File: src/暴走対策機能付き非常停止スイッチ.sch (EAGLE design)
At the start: 13 parts, among them T2 一般的なトランジスタ

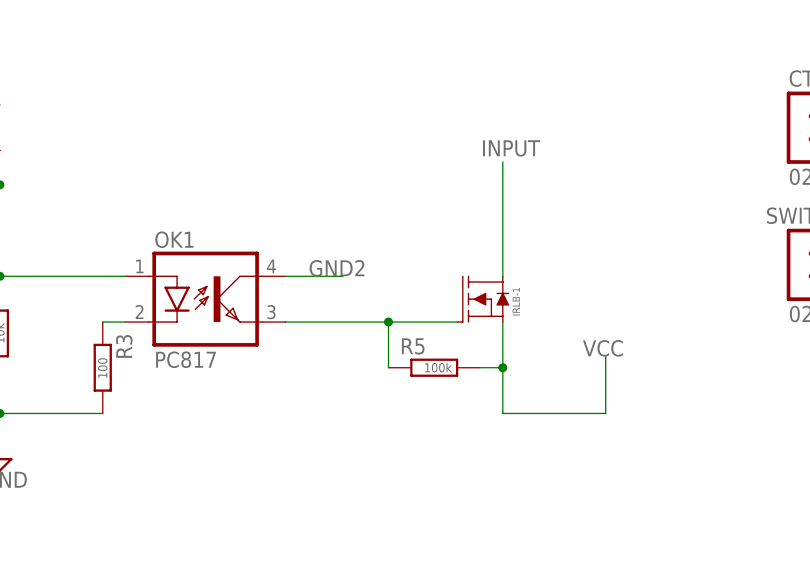
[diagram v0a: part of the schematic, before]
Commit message: 暴走対策機能付き非常停止スイッチの回路のガバを修復
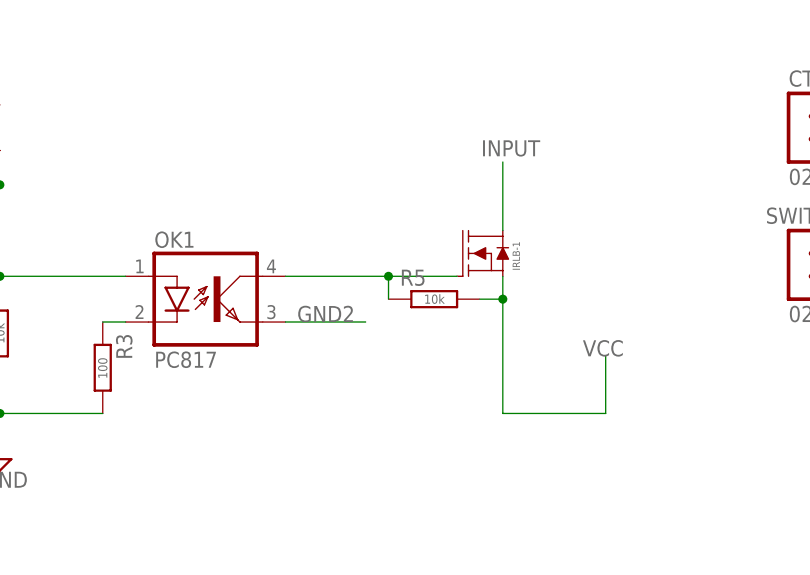
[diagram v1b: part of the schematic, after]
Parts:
- R5: value 100k -> 10k
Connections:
- net GND2: now also OK1.EMIT; no longer OK1.COL
- net N$8: now also OK1.COL; no longer OK1.EMIT
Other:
- moved on the sheet: IRLB-1, R5
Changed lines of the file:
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@@
 <part name="R6" library="rcl" library_urn="urn:adsk.eagle:library:334" deviceset="R-EU_" device="0204/7" package3d_urn="urn:adsk.eagle:package:23498/2" value="10k"/>
 <part name="IRLB-1" library="OKUDA_libraries" deviceset="IRLB3813" device="STAND"/>
-<part name="R5" library="rcl" library_urn="urn:adsk.eagle:library:334" deviceset="R-EU_" device="0204/7" package3d_urn="urn:adsk.eagle:package:23498/2" value="100k"/>
+<part name="R5" library="rcl" library_urn="urn:adsk.eagle:library:334" deviceset="R-EU_" device="0204/7" package3d_urn="urn:adsk.eagle:package:23498/2" value="10k"/>
 <part name="CTRL" library="con-jst-xh" deviceset="02-JST" device=""/>
 </parts>
@@
 <attribute name="VALUE" x="49.403" y="71.628" size="1.016" layer="96" rot="R180"/>
 </instance>
-<instance part="IRLB-1" gate="G$1" x="111.76" y="58.42" smashed="yes">
-<attribute name="NAME" x="113.665" y="56.515" size="0.8128" layer="95" rot="R90"/>
-</instance>
-<instance part="R5" gate="G$1" x="104.14" y="50.8" smashed="yes">
-<attribute name="NAME" x="100.33" y="52.2986" size="1.778" layer="95"/>
-<attribute name="VALUE" x="102.997" y="50.292" size="1.016" layer="96"/>
+<instance part="IRLB-1" gate="G$1" x="111.76" y="63.5" smashed="yes">
+<attribute name="NAME" x="113.665" y="61.595" size="0.8128" layer="95" rot="R90"/>
+</instance>
+<instance part="R5" gate="G$1" x="104.14" y="58.42" smashed="yes">
+<attribute name="NAME" x="100.33" y="59.9186" size="1.778" layer="95"/>
+<attribute name="VALUE" x="102.997" y="57.912" size="1.016" layer="96"/>
 </instance>
 <instance part="CTRL" gate="G$1" x="144.78" y="78.74" smashed="yes">
@@
 <segment>
 <pinref part="IRLB-1" gate="G$1" pin="S"/>
-<wire x1="111.76" y1="55.88" x2="111.76" y2="50.8" width="0.1524" layer="91"/>
-<wire x1="111.76" y1="50.8" x2="111.76" y2="45.72" width="0.1524" layer="91"/>
+<wire x1="111.76" y1="60.96" x2="111.76" y2="58.42" width="0.1524" layer="91"/>
+<wire x1="111.76" y1="58.42" x2="111.76" y2="45.72" width="0.1524" layer="91"/>
 <wire x1="111.76" y1="45.72" x2="123.19" y2="45.72" width="0.1524" layer="91"/>
 <wire x1="123.19" y1="45.72" x2="123.19" y2="52.07" width="0.1524" layer="91"/>
 <label x="120.65" y="52.07" size="1.778" layer="95"/>
 <pinref part="R5" gate="G$1" pin="2"/>
-<wire x1="109.22" y1="50.8" x2="111.76" y2="50.8" width="0.1524" layer="91"/>
-<junction x="111.76" y="50.8"/>
+<wire x1="109.22" y1="58.42" x2="111.76" y2="58.42" width="0.1524" layer="91"/>
+<junction x="111.76" y="58.42"/>
 </segment>
 </net>
 <net name="N$8" class="0">
 <segment>
-<pinref part="OK1" gate="A" pin="EMIT"/>
 <pinref part="IRLB-1" gate="G$1" pin="G"/>
-<wire x1="87.63" y1="55.88" x2="99.06" y2="55.88" width="0.1524" layer="91"/>
 <pinref part="R5" gate="G$1" pin="1"/>
-<wire x1="99.06" y1="55.88" x2="106.68" y2="55.88" width="0.1524" layer="91"/>
-<wire x1="99.06" y1="50.8" x2="99.06" y2="55.88" width="0.1524" layer="91"/>
-<junction x="99.06" y="55.88"/>
+<wire x1="99.06" y1="60.96" x2="106.68" y2="60.96" width="0.1524" layer="91"/>
+<wire x1="99.06" y1="58.42" x2="99.06" y2="60.96" width="0.1524" layer="91"/>
+<junction x="99.06" y="60.96"/>
+<pinref part="OK1" gate="A" pin="COL"/>
+<wire x1="99.06" y1="60.96" x2="87.63" y2="60.96" width="0.1524" layer="91"/>
 </segment>
 </net>
@@
 <label x="109.347" y="74.295" size="1.778" layer="95"/>
 <pinref part="IRLB-1" gate="G$1" pin="D"/>
-<wire x1="111.76" y1="60.96" x2="111.76" y2="73.66" width="0.1524" layer="91"/>
+<wire x1="111.76" y1="66.04" x2="111.76" y2="73.66" width="0.1524" layer="91"/>
 </segment>
 </net>
@@
 </segment>
 <segment>
-<pinref part="OK1" gate="A" pin="COL"/>
-<wire x1="87.63" y1="60.96" x2="93.98" y2="60.96" width="0.1524" layer="91"/>
-<label x="90.17" y="60.96" size="1.778" layer="95"/>
-</segment>
-</net>
+<pinref part="OK1" gate="A" pin="EMIT"/>
+<wire x1="87.63" y1="55.88" x2="96.52" y2="55.88" width="0.1524" layer="91"/>
+<label x="88.9" y="55.88" size="1.778" layer="95"/>
+</segment>
+</net>
